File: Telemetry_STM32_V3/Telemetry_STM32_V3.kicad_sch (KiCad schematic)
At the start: 56 parts, among them J1 USB_B_Micro, J2 Conn_01x04_Socket, J3 Conn_01x02_Socket, J4 Conn_ARM_SWD_TagConnect_TC2030, J5 Conn_01x02_Socket, U1 STM32F405RGT6, U2 MIC37100-3.3WS, U3 USBLC6-2SC6, U4 24LC01BT-E/LT, U5 SN65HVD230, U6 RFM95W, U7 RFM95W, U8 RFM95W, U9 RFM95W, Y1 12MHz

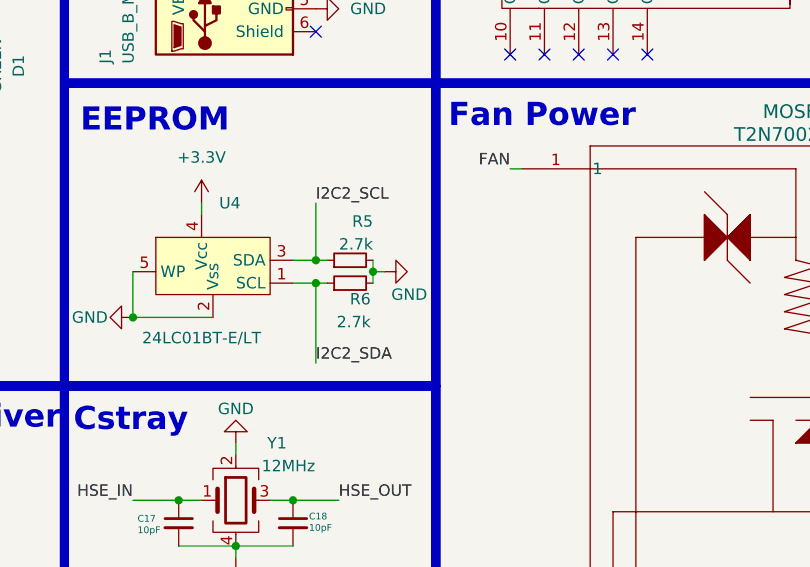
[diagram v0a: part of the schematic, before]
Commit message: Last minute board fixes.
Changed I2C pull down resistors to pull up on Telemetry and IMU.
Improved routing of NRST pin on IMU.
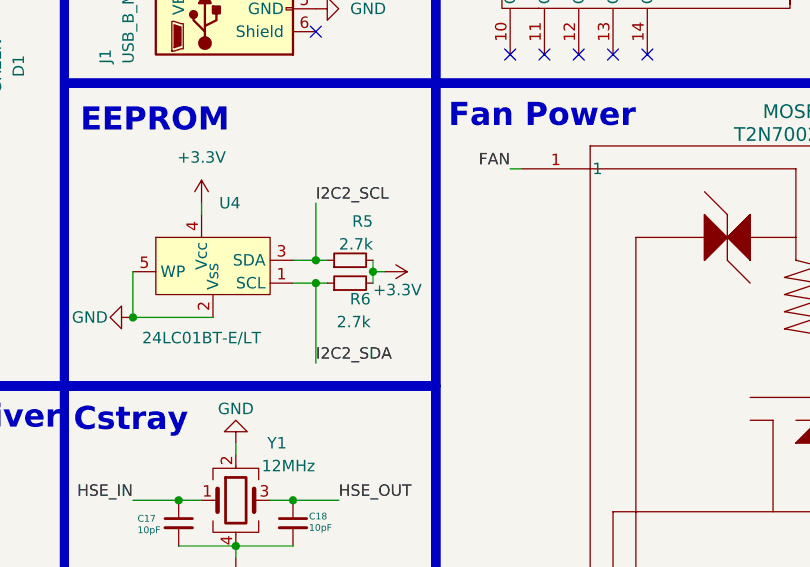
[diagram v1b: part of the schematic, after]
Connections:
- net +3.3V: now also R5.2, R6.2
- net GND: no longer R5.2, R6.2
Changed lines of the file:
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@@
 	)
 	(symbol
+		(lib_id "power:+3.3V")
+		(at 135.89 116.84 270)
+		(unit 1)
+		(exclude_from_sim no)
+		(in_bom yes)
+		(on_board yes)
+		(dnp no)
+		(property "Reference" "#PWR020"
+			(at 132.08 116.84 0)
+			(effects
+				(font
+					(size 1.27 1.27)
+				)
+				(hide yes)
+			)
+		)
+		(property "Value" "+3.3V"
+			(at 134.62 118.872 90)
+			(effects
+				(font
+					(size 1.27 1.27)
+				)
+				(justify left)
+			)
+		)
+		(property "Footprint" ""
+			(at 135.89 116.84 0)
+			(effects
+				(font
+					(size 1.27 1.27)
+				)
+				(hide yes)
+			)
+		)
+		(property "Datasheet" ""
+			(at 135.89 116.84 0)
+			(effects
+				(font
+					(size 1.27 1.27)
+				)
+				(hide yes)
+			)
+		)
+		(property "Description" ""
+			(at 135.89 116.84 0)
+			(effects
+				(font
+					(size 1.27 1.27)
+				)
+				(hide yes)
+			)
+		)
+		(pin "1"
+		)
+		(instances
+			(project "Telemetry_STM32_V3"
+				(path "/10642104-ca4c-424b-9529-4a50f3c6aa32"
+					(reference "#PWR020")
+					(unit 1)
+				)
+			)
+		)
+	)
+	(symbol
 		(lib_id "power:VCC")
 		(at 193.04 25.4 0)
@@
 					(unit 1)
 				)
-			)
-		)
-	)
-	(symbol
-		(lib_id "power:GND")
-		(at 135.89 116.84 90)
-		(unit 1)
-		(exclude_from_sim no)
-		(in_bom yes)
-		(on_board yes)
-		(dnp no)
-		(property "Reference" "#PWR020"
-			(at 142.24 116.84 0)
-			(effects
-				(font
-					(size 1.27 1.27)
-				)
-				(hide yes)
-			)
-		)
-		(property "Value" "GND"
-			(at 136.652 119.38 90)
-			(effects
-				(font
-					(size 1.27 1.27)
-				)
-				(justify right)
-			)
-		)
-		(property "Footprint" ""
-			(at 135.89 116.84 0)
-			(effects
-				(font
-					(size 1.27 1.27)
-				)
-				(hide yes)
-			)
-		)
-		(property "Datasheet" ""
-			(at 135.89 116.84 0)
-			(effects
-				(font
-					(size 1.27 1.27)
-				)
-				(hide yes)
-			)
-		)
-		(property "Description" "Power symbol creates a global label with name \"GND\" , ground"
-			(at 135.89 116.84 0)
-			(effects
-				(font
-					(size 1.27 1.27)
-				)
-				(hide yes)
-			)
-		)
-		(pin "1"
-		)
-		(instances
-			(project "Telemetry_STM32_V3"
-				(path "/10642104-ca4c-424b-9529-4a50f3c6aa32"
-					(reference "#PWR020")
-					(unit 1)
-				)

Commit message: Telemetry - CAN, I2C, USB Fix
Fr this time
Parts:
- removed J3: Conn_01x02_Socket, symbol Connector:Conn_01x02_Socket
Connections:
- net +3.3V: now also D1.2 (A); no longer D1.1 (K)
- net CRX: now also U1.33 (PB12), U5.4 (R); no longer U1.34 (PB13), U5.1 (D)
- net CS_2: now also U1.28 (PB2); no longer U1.33 (PB12)
- net CTX: now also U1.34 (PB13), U5.1 (D); no longer U1.35 (PB14), U5.4 (R)
- net I2C2_SCL: now also R6.1, U4.1 (SCL); no longer R5.1, U4.3 (SDA)
- net I2C2_SDA: now also R5.1, U4.3 (SDA); no longer R6.1, U4.1 (SCL)
- net USB_D+: now also U3.6 (I/O1); no longer U3.4 (I/O2)
- net USB_D-: now also U3.4 (I/O2); no longer U3.6 (I/O1)
- net at R2.1: now also D1.1 (K); no longer D1.2 (A)
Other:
- moved on the sheet: D1
